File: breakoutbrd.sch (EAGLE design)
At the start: 6 parts

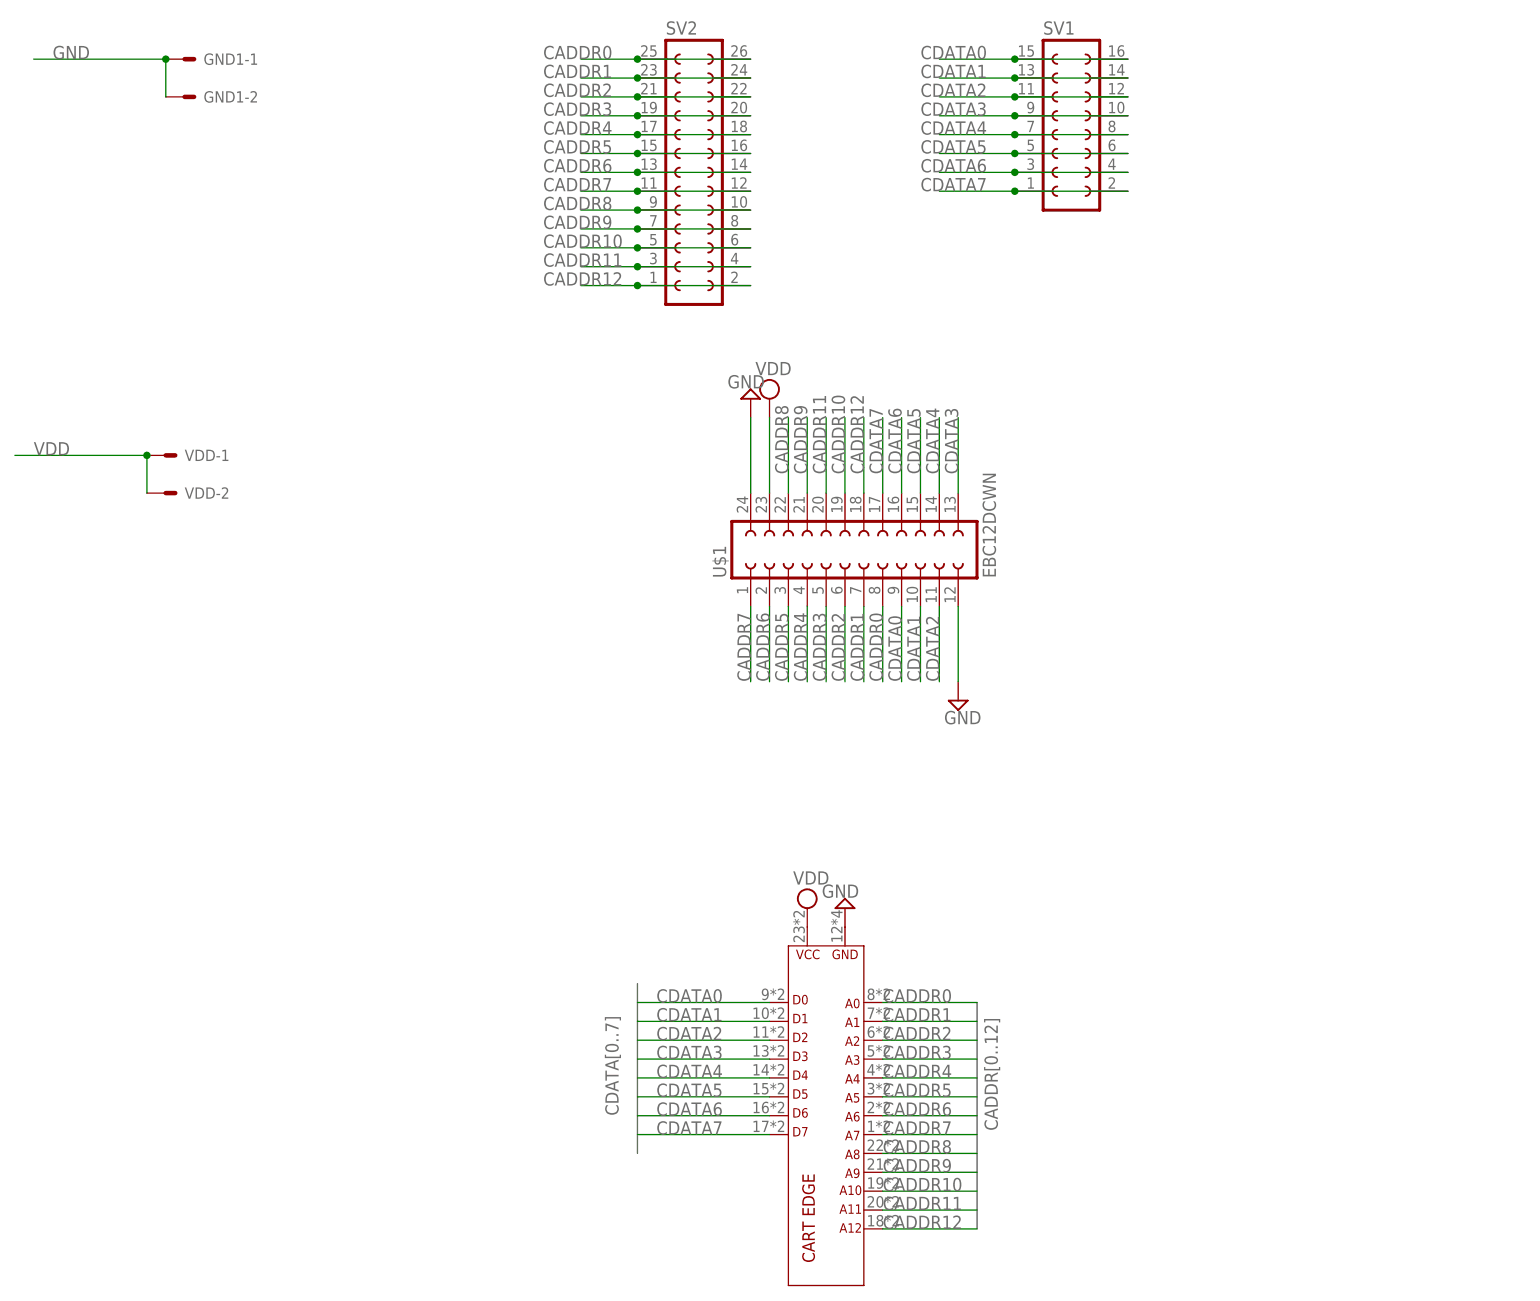
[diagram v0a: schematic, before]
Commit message: Rework board to drive an STM32F4XX DevEBox from the cartridge edge
Keep only the lower edge fingers and their stubs; remove SV1, SV2, the
VDD/GND Molex headers, the U$1 socket, the top fingers, mounting holes,
ground pour and old labels. Flatten the top edge (tabs removed) at
y=83.82mm.

Add footprint U1 (STM32F4XX_DEVEBOX): the DevEBox rotated 90 deg CCW,
with 1.0mm through-holes at the matched header pins and its four 3.2mm
mounting holes. Route D0-D7 -> PD8-PD15, A0-A12 -> PE0-PE12, VDD -> 5V
and GND -> GND, and join the two GND fingers.

Schematic and library updated to match (parts removed, J1 limited to
pads 1-24, STM part added). Preview in breakout_stm_overlay.png.

Co-Authored-By: Claude Opus 5.5 <noreply@anthropic.com>
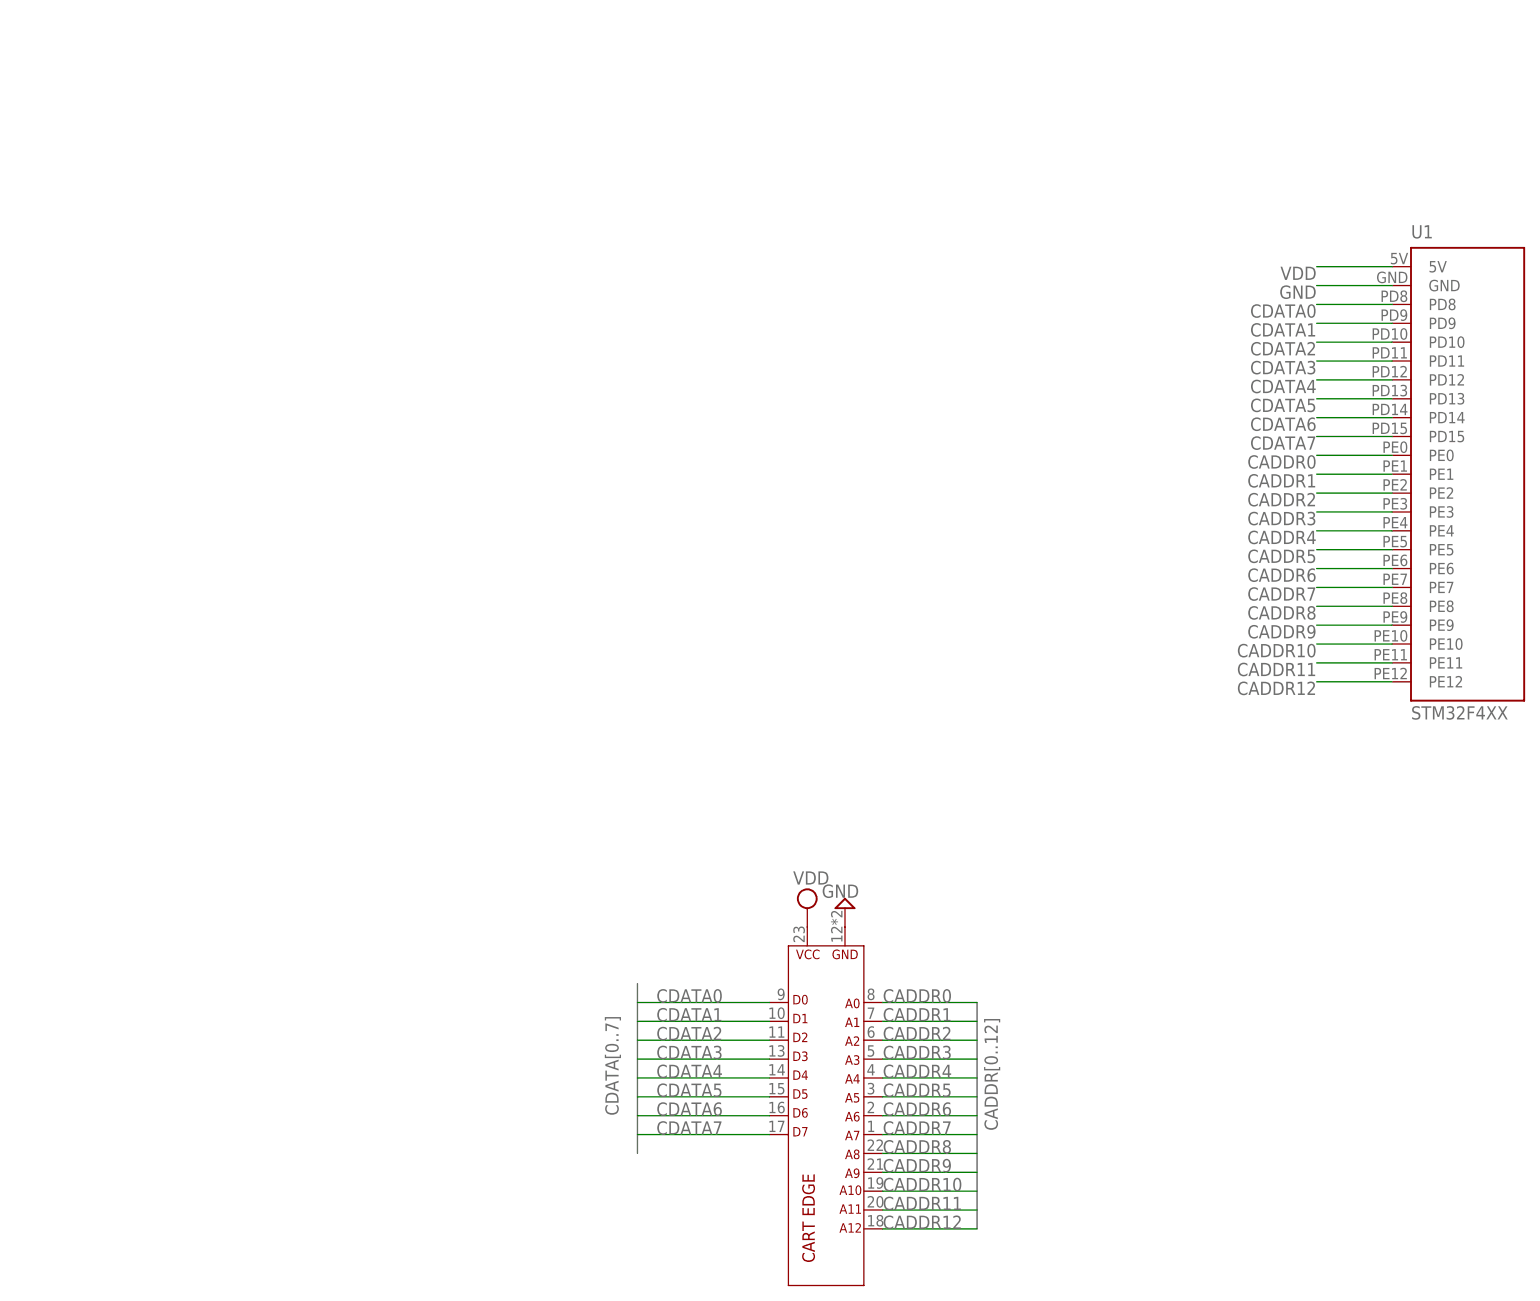
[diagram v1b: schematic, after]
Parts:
- removed GND1, VDD: 22-23-2021, a26board:22-23-2021
- removed SV1: (no value), a26board:FE08-2
- removed SV2: (no value), a26board:FE13-2
- removed U$1: EBC12DCWN, a26board:EBC12DCWN
- added U1: STM32F4XX, a26board:STM32F4XX_DEVEBOX
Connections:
- net CADDR0: now also U1.PE0; no longer SV2.25, SV2.26, U$1.8
- net CADDR1: now also U1.PE1; no longer SV2.23, SV2.24, U$1.7
- net CADDR10: now also U1.PE10; no longer SV2.5, SV2.6, U$1.19
- net CADDR11: now also U1.PE11; no longer SV2.3, SV2.4, U$1.20
- net CADDR12: now also U1.PE12; no longer SV2.1, SV2.2, U$1.18
- net CADDR2: now also U1.PE2; no longer SV2.21, SV2.22, U$1.6
- net CADDR3: now also U1.PE3; no longer SV2.19, SV2.20, U$1.5
- net CADDR4: now also U1.PE4; no longer SV2.17, SV2.18, U$1.4
- net CADDR5: now also U1.PE5; no longer SV2.15, SV2.16, U$1.3
- net CADDR6: now also U1.PE6; no longer SV2.13, SV2.14, U$1.2
- net CADDR7: now also U1.PE7; no longer SV2.11, SV2.12, U$1.1
- net CADDR8: now also U1.PE8; no longer SV2.10, SV2.9, U$1.22
- net CADDR9: now also U1.PE9; no longer SV2.7, SV2.8, U$1.21
- net CDATA0: now also U1.PD8; no longer SV1.15, SV1.16, U$1.9
- net CDATA1: now also U1.PD9; no longer SV1.13, SV1.14, U$1.10
- net CDATA2: now also U1.PD10; no longer SV1.11, SV1.12, U$1.11
- net CDATA3: now also U1.PD11; no longer SV1.10, SV1.9, U$1.13
- net CDATA4: now also U1.PD12; no longer SV1.7, SV1.8, U$1.14
- net CDATA5: now also U1.PD13; no longer SV1.5, SV1.6, U$1.15
- net CDATA6: now also U1.PD14; no longer SV1.3, SV1.4, U$1.16
- net CDATA7: now also U1.PD15; no longer SV1.1, SV1.2, U$1.17
- net GND: now also U1.GND; no longer GND1-1.S, GND1-2.S, U$1.12, U$1.24
- net VDD: now also U1.5V; no longer U$1.23, VDD-1.S, VDD-2.S
